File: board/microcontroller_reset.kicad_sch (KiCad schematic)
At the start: 4 parts, among them SW501 RST

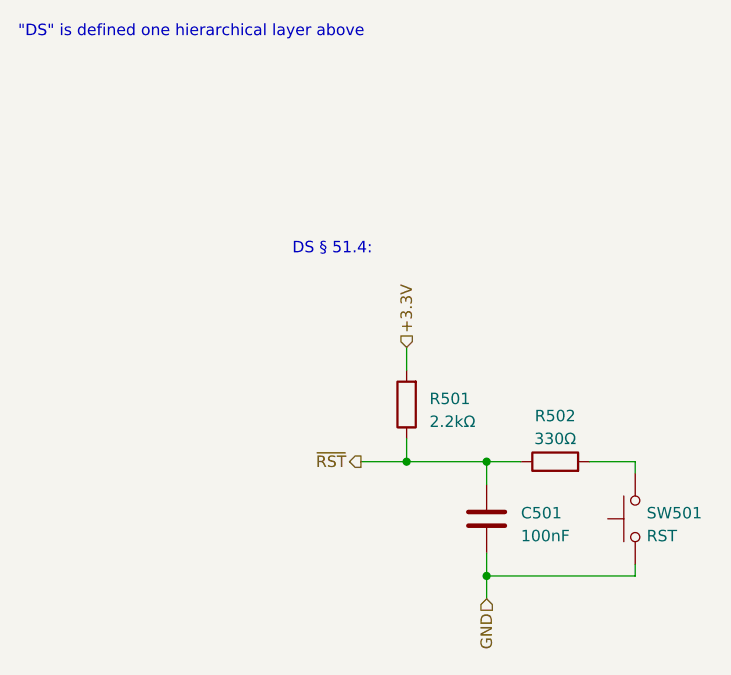
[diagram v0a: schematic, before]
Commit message: redo board with STM32G0B0CET
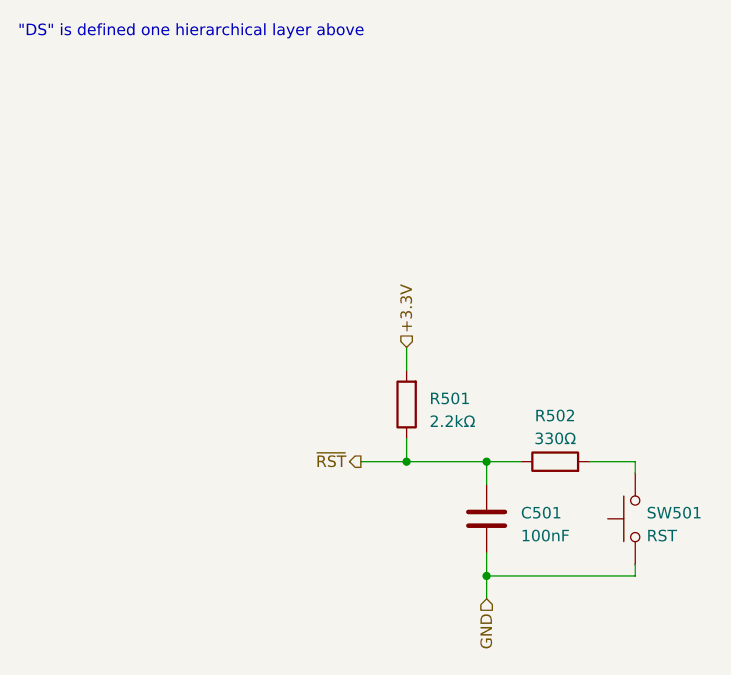
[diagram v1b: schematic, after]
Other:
- note removed: "DS § 51.4:"
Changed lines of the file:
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@@
     (stroke (width 0) (type default))
-  )
-  (text "DS § 51.4:" (at 45.72 41.91 0)
-    (effects (font (size 1.27 1.27)) (justify left bottom))
   )
   (text "\"DS\" is defined one hierarchical layer above" (at 15.24 17.78 0)
